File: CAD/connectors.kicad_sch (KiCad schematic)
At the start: 2 parts, among them J1 Conn_02x04_Odd_Even, J2 Conn_02x04_Odd_Even

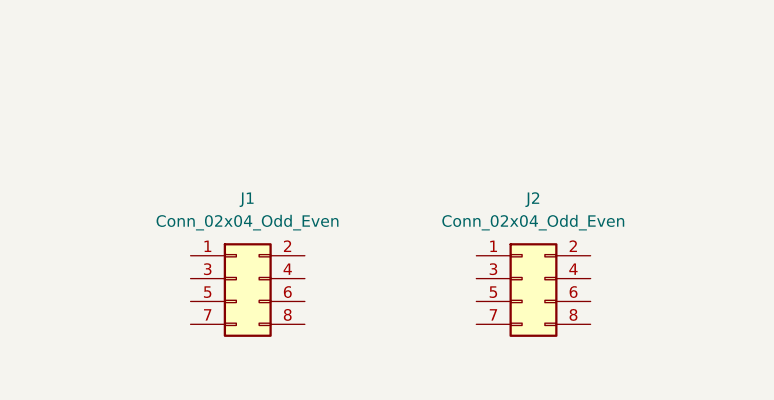
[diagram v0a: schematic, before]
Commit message: Add Block A connectors
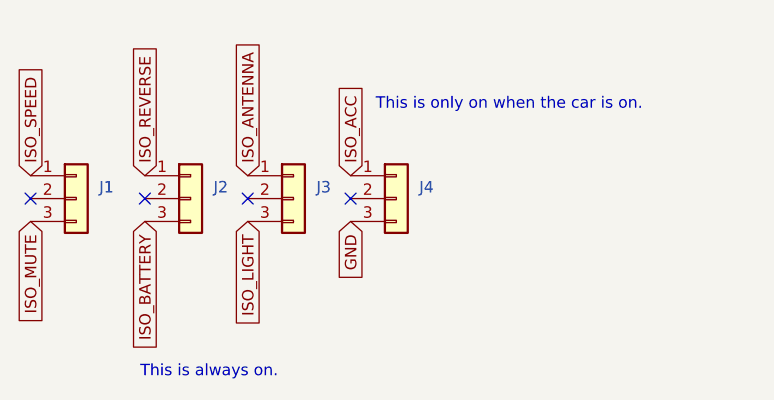
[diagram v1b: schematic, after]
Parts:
- removed J1, J2: Conn_02x04_Odd_Even, symbol Connector_Generic:Conn_02x04_Odd_Even
- added J1, J2, J3, J4: Conn_01x03, Connector_PinHeader_2.54mm:PinHeader_1x03_P2.54mm_Vertical, symbol Connector_Generic:Conn_01x03
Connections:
- new net GND: J4.3 (Pin_3)
- new net ISO_ACC: J4.1 (Pin_1)
- new net ISO_ANTENNA: J3.1 (Pin_1)
- new net ISO_BATTERY: J2.3 (Pin_3)
- new net ISO_LIGHT: J3.3 (Pin_3)
- new net ISO_MUTE: J1.3 (Pin_3)
- new net ISO_REVERSE: J2.1 (Pin_1)
- new net ISO_SPEED: J1.1 (Pin_1)
- no-connect marks 0 -> 4
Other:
- note added: "This is always on."
- note added: "This is only on when the car is on."
